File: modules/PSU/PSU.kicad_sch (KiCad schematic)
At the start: 8 parts, among them J1 Conn_01x01_Pin, J2 Conn_01x02_Pin, Q10 MMBT3904

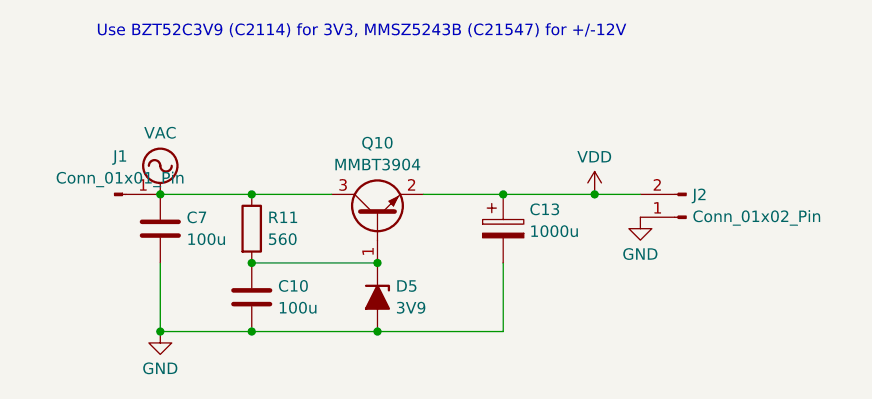
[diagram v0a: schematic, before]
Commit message: PSU: added power led
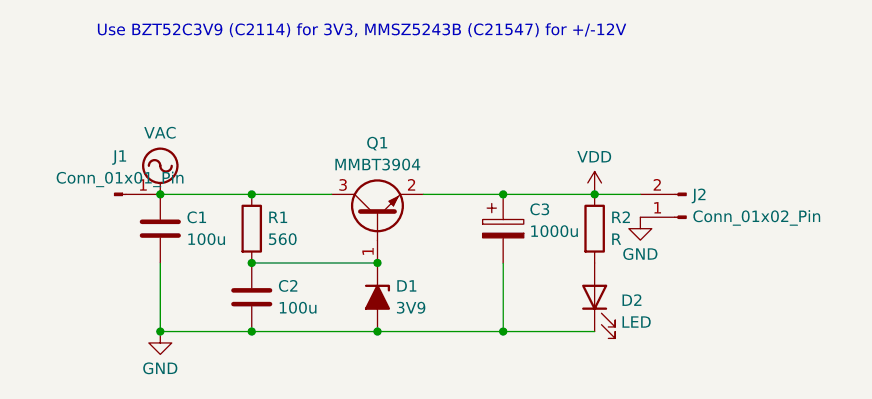
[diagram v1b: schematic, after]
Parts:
- added D2: LED, LED_SMD:LED_0603_1608Metric, symbol Device:LED
- added R2: R, Resistor_SMD:R_0603_1608Metric, symbol Device:R
- J1, J2: now left out of the parts list
- renumbered C7 to C1, C10 to C2, C13 to C3, D5 to D1, Q10 to Q1, R11 to R1
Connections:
- net GND: now also D2.1 (K)
- net VDD: now also R2.1
- new net: D2.2 (A), R2.2
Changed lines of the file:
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@@
+	)
+	(junction
+		(at 134.62 80.01)
+		(diameter 0)
+		(color 0 0 0 0)
 	)
 	(junction
@@
 	(wire
 		(pts
-			(xy 134.62 72.39) (xy 134.62 80.01)
+			(xy 134.62 80.01) (xy 144.78 80.01)
 		)
 		(stroke
@@
 	(wire
 		(pts
-			(xy 125.73 64.77) (xy 134.62 64.77)
+			(xy 134.62 72.39) (xy 134.62 80.01)
 		)
 		(stroke
@@
 	(wire
 		(pts
-			(xy 106.68 64.77) (xy 115.57 64.77)
+			(xy 125.73 64.77) (xy 134.62 64.77)
 		)
 		(stroke
@@
 	(wire
 		(pts
-			(xy 106.68 80.01) (xy 96.52 80.01)
+			(xy 106.68 64.77) (xy 115.57 64.77)
 		)
 		(stroke
@@
 	(wire
 		(pts
-			(xy 134.62 64.77) (xy 144.78 64.77)
+			(xy 106.68 80.01) (xy 96.52 80.01)
 		)
 		(stroke
@@
 	(wire
 		(pts
-			(xy 120.65 80.01) (xy 106.68 80.01)
+			(xy 134.62 64.77) (xy 144.78 64.77)
 		)
 		(stroke
@@
 	(wire
 		(pts
-			(xy 144.78 64.77) (xy 149.86 64.77)
+			(xy 120.65 80.01) (xy 106.68 80.01)
 		)
 		(stroke
@@
 	(wire
 		(pts
-			(xy 96.52 64.77) (xy 106.68 64.77)
+			(xy 144.78 64.77) (xy 149.86 64.77)
 		)
 		(stroke
@@
 	(wire
 		(pts
-			(xy 96.52 80.01) (xy 96.52 72.39)
+			(xy 96.52 64.77) (xy 106.68 64.77)
 		)
 		(stroke
@@
 		)
 	)
+	(wire
+		(pts
+			(xy 96.52 80.01) (xy 96.52 72.39)
+		)
+		(stroke
+			(width 0)
+			(type default)
+		)
+	)
 	(symbol
 		(lib_id "Transistor_BJT:MMBT3904")
@@
 		(dnp no)
 		(fields_autoplaced yes)
-		(property "Reference" "Q10"
+		(property "Reference" "Q1"
 			(at 120.65 59.0761 90)
 			(effects
@@
 			(project "PSU"
 				(path "/da8feed1-a20b-452e-b8e4-5030f9f67fed"
-					(reference "Q10")
+					(reference "Q1")
 					(unit 1)
 				)
@@
 		(dnp no)
 		(fields_autoplaced yes)
-		(property "Reference" "C7"
+		(property "Reference" "C1"
 			(at 99.441 67.3678 0)
 			(effects
@@
 			(project "PSU"
 				(path "/da8feed1-a20b-452e-b8e4-5030f9f67fed"
-					(reference "C7")
+					(reference "C1")
 					(unit 1)
 				)
@@
 		(unit 1)
 		(exclude_from_sim no)
-		(in_bom yes)
+		(in_bom no)
 		(on_board yes)
 		(dnp no)
@@
 		(dnp no)
 		(fields_autoplaced yes)
-		(property "Reference" "C10"
+		(property "Reference" "C2"
 			(at 109.601 74.9878 0)
 			(effects
@@
 			(project "PSU"
 				(path "/da8feed1-a20b-452e-b8e4-5030f9f67fed"
-					(reference "C10")
+					(reference "C2")
 					(unit 1)
 				)
@@
 		(unit 1)
 		(exclude_from_sim no)
-		(in_bom yes)
+		(in_bom no)
 		(on_board yes)
 		(dnp no)
@@
 	)
 	(symbol
+		(lib_id "Device:LED")
+		(at 144.78 76.2 90)
+		(unit 1)
+		(exclude_from_sim no)
+		(in_bom no)
+		(on_board yes)
+		(dnp no)
+		(fields_autoplaced yes)
+		(property "Reference" "D2"
+			(at 147.701 76.5753 90)
+			(effects
+				(font
+					(size 1.27 1.27)
+				)
+				(justify right)
+			)
+		)
+		(property "Value" "LED"
+			(at 147.701 78.9996 90)
+			(effects
+				(font
+					(size 1.27 1.27)
+				)
+				(justify right)
+			)
+		)
+		(property "Footprint" "LED_SMD:LED_0603_1608Metric"
+			(at 144.78 76.2 0)
+			(effects
+				(font
+					(size 1.27 1.27)
+				)
+				(hide yes)
+			)
+		)
+		(property "Datasheet" "~"
+			(at 144.78 76.2 0)
+			(effects
+				(font
+					(size 1.27 1.27)
+				)
+				(hide yes)
+			)
+		)
+		(property "Description" "Light emitting diode"
+			(at 144.78 76.2 0)
+			(effects
+				(font
+					(size 1.27 1.27)
+				)
+				(hide yes)
+			)
+		)
+		(property "Sim.Pins" "1=K 2=A"
+			(at 144.78 76.2 0)
+			(effects
+				(font
+					(size 1.27 1.27)
+				)
+				(hide yes)
+			)
+		)
+		(pin "1"
+		)
+		(pin "2"
+		)
+		(instances
+			(project ""
+				(path "/da8feed1-a20b-452e-b8e4-5030f9f67fed"
+					(reference "D2")
+					(unit 1)
+				)
+			)
+		)
+	)
+	(symbol
+		(lib_id "Device:R")
+		(at 144.78 68.58 0)
+		(unit 1)
+		(exclude_from_sim no)
+		(in_bom no)
+		(on_board yes)
+		(dnp no)
+		(fields_autoplaced yes)
+		(property "Reference" "R2"
+			(at 146.558 67.3678 0)
+			(effects
+				(font
+					(size 1.27 1.27)
+				)
+				(justify left)
+			)
+		)
+		(property "Value" "R"
+			(at 146.558 69.7921 0)
+			(effects
+				(font
+					(size 1.27 1.27)
+				)
+				(justify left)
+			)
+		)
+		(property "Footprint" "Resistor_SMD:R_0603_1608Metric"
+			(at 143.002 68.58 90)
+			(effects
+				(font
+					(size 1.27 1.27)
+				)
+				(hide yes)
+			)
+		)
+		(property "Datasheet" "~"
+			(at 144.78 68.58 0)
+			(effects
+				(font
+					(size 1.27 1.27)
+				)
+				(hide yes)
+			)
+		)
+		(property "Description" "Resistor"
+			(at 144.78 68.58 0)
+			(effects
+				(font
+					(size 1.27 1.27)
+				)
+				(hide yes)
+			)
+		)
+		(pin "2"
+		)
+		(pin "1"
+		)
+		(instances
+			(project ""
+				(path "/da8feed1-a20b-452e-b8e4-5030f9f67fed"
+					(reference "R2")
+					(unit 1)
+				)
+			)
+		)
+	)
+	(symbol
 		(lib_id "power:GND")
 		(at 96.52 80.01 0)
@@
 		(dnp no)
 		(fields_autoplaced yes)
-		(property "Reference" "#PWR08"
+		(property "Reference" "#PWR02"
 			(at 96.52 86.36 0)
 			(effects
@@
 			(project "PSU"
 				(path "/da8feed1-a20b-452e-b8e4-5030f9f67fed"
-					(reference "#PWR08")
+					(reference "#PWR02")
 					(unit 1)
 				)
@@
 		(dnp no)
 		(fields_autoplaced yes)
-		(property "Reference" "D5"
+		(property "Reference" "D1"
 			(at 122.682 74.9878 90)
 			(effects
@@
 			(project "PSU"
 				(path "/da8feed1-a20b-452e-b8e4-5030f9f67fed"
-					(reference "D5")
+					(reference "D1")
 					(unit 1)
 				)
@@
 		(dnp no)
 		(fields_autoplaced yes)
-		(property "Reference" "#PWR01"
+		(property "Reference" "#PWR03"
 			(at 144.78 68.58 0)
 			(effects
@@
 			(project ""
 				(path "/da8feed1-a20b-452e-b8e4-5030f9f67fed"
-					(reference "#PWR01")
+					(reference "#PWR03")
 					(unit 1)
 				)
@@
 		(dnp no)
 		(fields_autoplaced yes)
-		(property "Reference" "#PWR02"
+		(property "Reference" "#PWR01"
 			(at 96.52 67.31 0)
 			(effects
@@
 			(project ""
 				(path "/da8feed1-a20b-452e-b8e4-5030f9f67fed"
-					(reference "#PWR02")
+					(reference "#PWR01")
 					(unit 1)
 				)
@@
 		(dnp no)
 		(fields_autoplaced yes)
-		(property "Reference" "#PWR03"
+		(property "Reference" "#PWR04"
 			(at 149.86 73.66 0)
 			(effects
@@
 			(project "PSU"
 				(path "/da8feed1-a20b-452e-b8e4-5030f9f67fed"
-					(reference "#PWR03")
+					(reference "#PWR04")
 					(unit 1)
 				)
@@
 		(dnp no)
 		(fields_autoplaced yes)
-		(property "Reference" "C13"
+		(property "Reference" "C3"
 			(at 137.541 66.4788 0)
 			(effects
@@
 			(project "PSU"
 				(path "/da8feed1-a20b-452e-b8e4-5030f9f67fed"
-					(reference "C13")
+					(reference "C3")
 					(unit 1)
 				)
@@
 		(dnp no)
 		(fields_autoplaced yes)
-		(property "Reference" "R11"
+		(property "Reference" "R1"
 			(at 108.458 67.3678 0)
 			(effects
@@
 			(project "PSU"
 				(path "/da8feed1-a20b-452e-b8e4-5030f9f67fed"
-					(reference "R11")
-					(unit 1)
-				)
+					(reference "R1")
+					(unit 1)
+				)
